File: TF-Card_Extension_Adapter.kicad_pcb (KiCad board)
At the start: 2 copper layers, 28.6 x 30.9 mm, 3 parts, among them J1 Conn_01x08_Pin, J2 TF_Card_Slot, J3 TF_Card

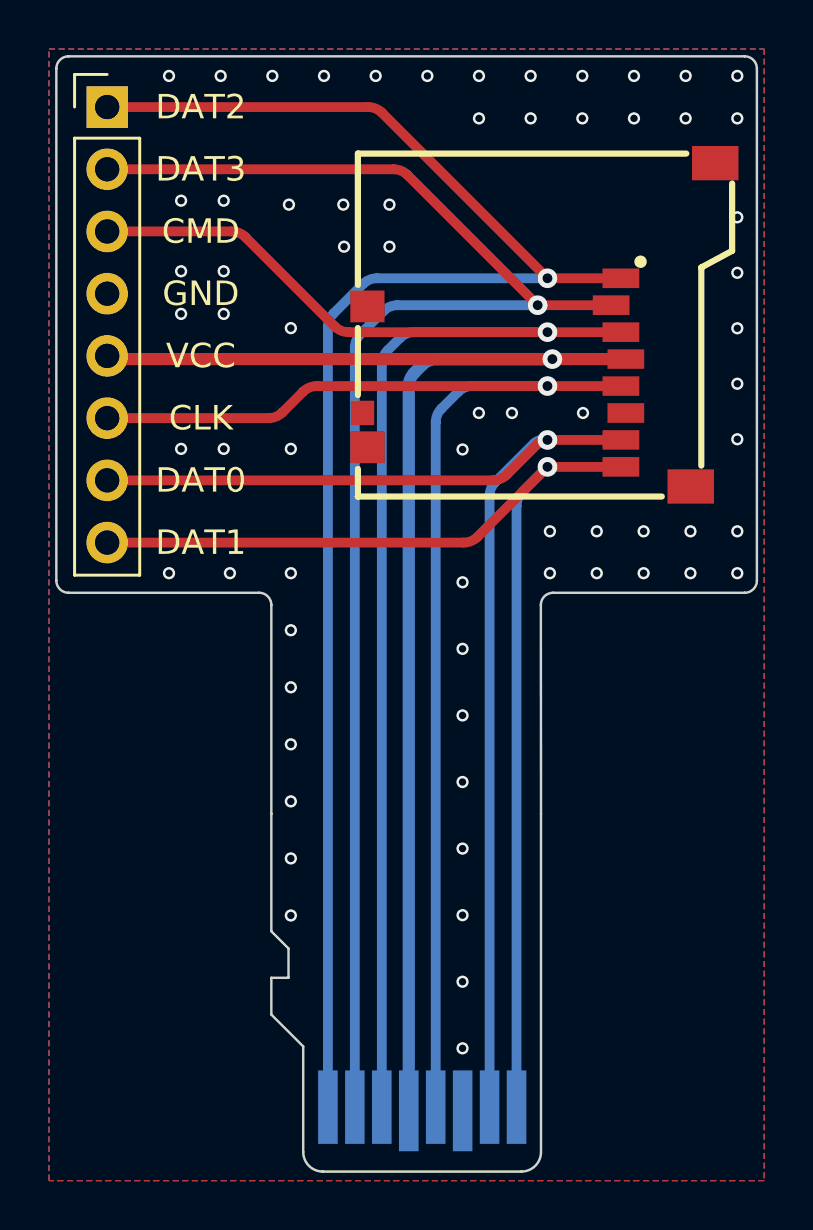
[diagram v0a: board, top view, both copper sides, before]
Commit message: feat: Adjust SDIO wiring to equal length
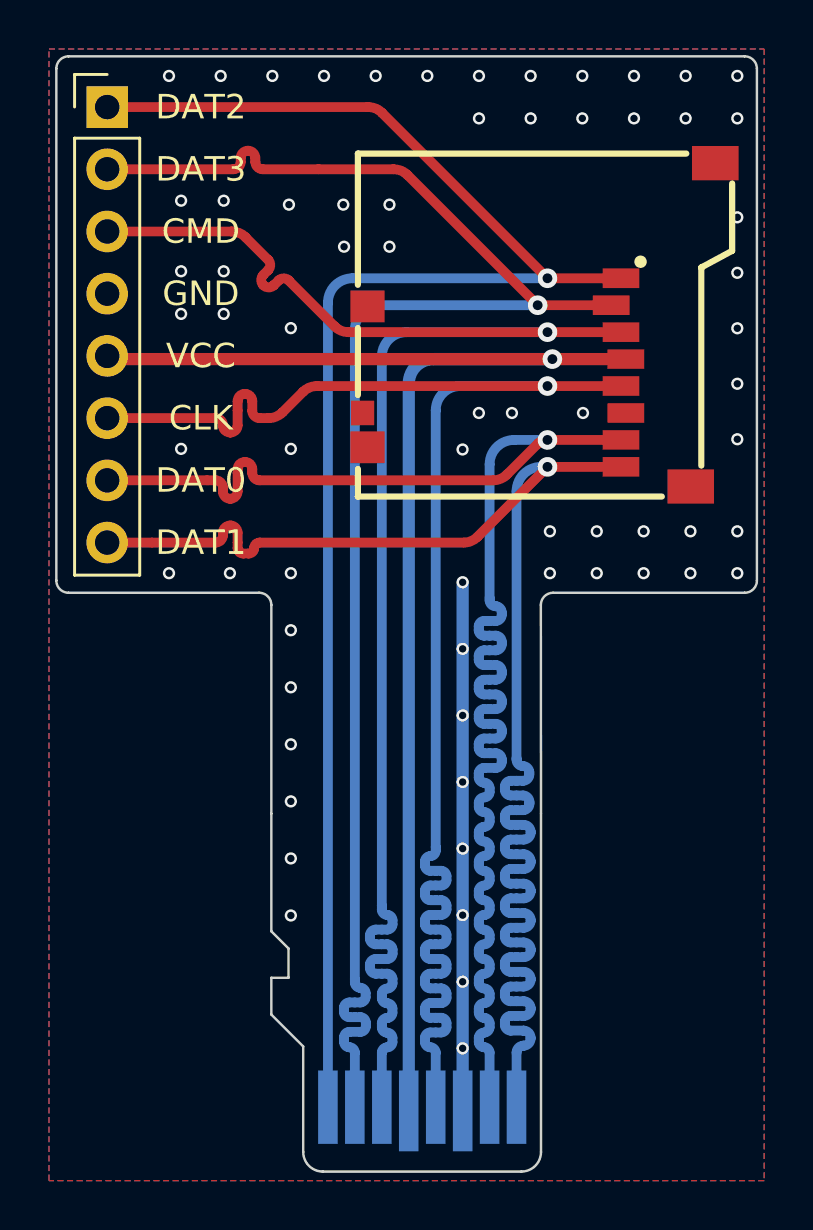
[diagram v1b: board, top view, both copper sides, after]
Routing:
- net GND: track 0.00 -> 21.6 mm, vias 69 -> 68
- net Net-(J1-Pin_8): track 48.8 -> 65.7 mm
- net Net-(J1-Pin_7): track 50.0 -> 65.5 mm
- net Net-(J1-Pin_5): track 54.7 -> 65.8 mm
- net Net-(J1-Pin_3): track 60.4 -> 65.9 mm
- net Net-(J1-Pin_2): track 62.1 -> 66.0 mm
- net Net-(J1-Pin_1): track 65.6 -> 66.2 mm
